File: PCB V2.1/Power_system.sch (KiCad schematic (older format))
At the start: 18 parts, among them J3 B2B-PH-K-S(LF)(SN), J4 B3B-PH-K-S(LF)(SN), Q1 DMG2307L-7, Q2 DMG2307L-7, U2 BQ24210DQCT, U3 AZ1117CR-3.3TRG1_1

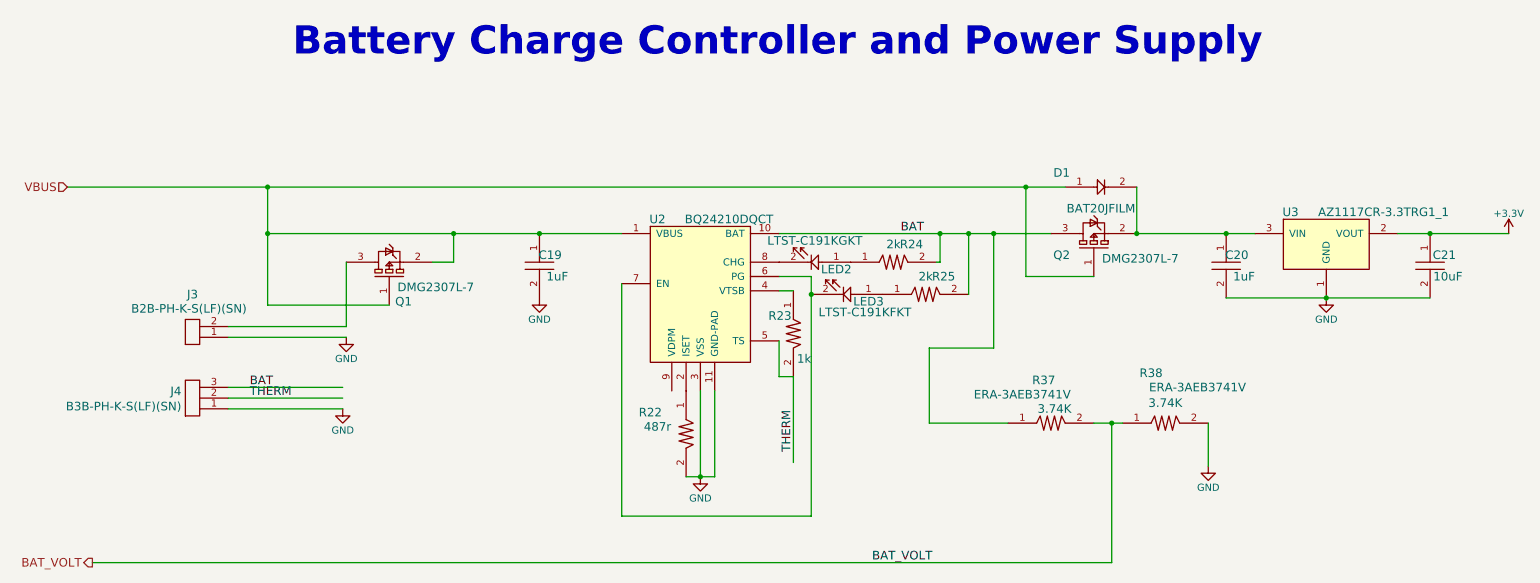
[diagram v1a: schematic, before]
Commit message: Test Points
Test points added as well as some retooling of the PCB overall. More
updates to come before the pending fab
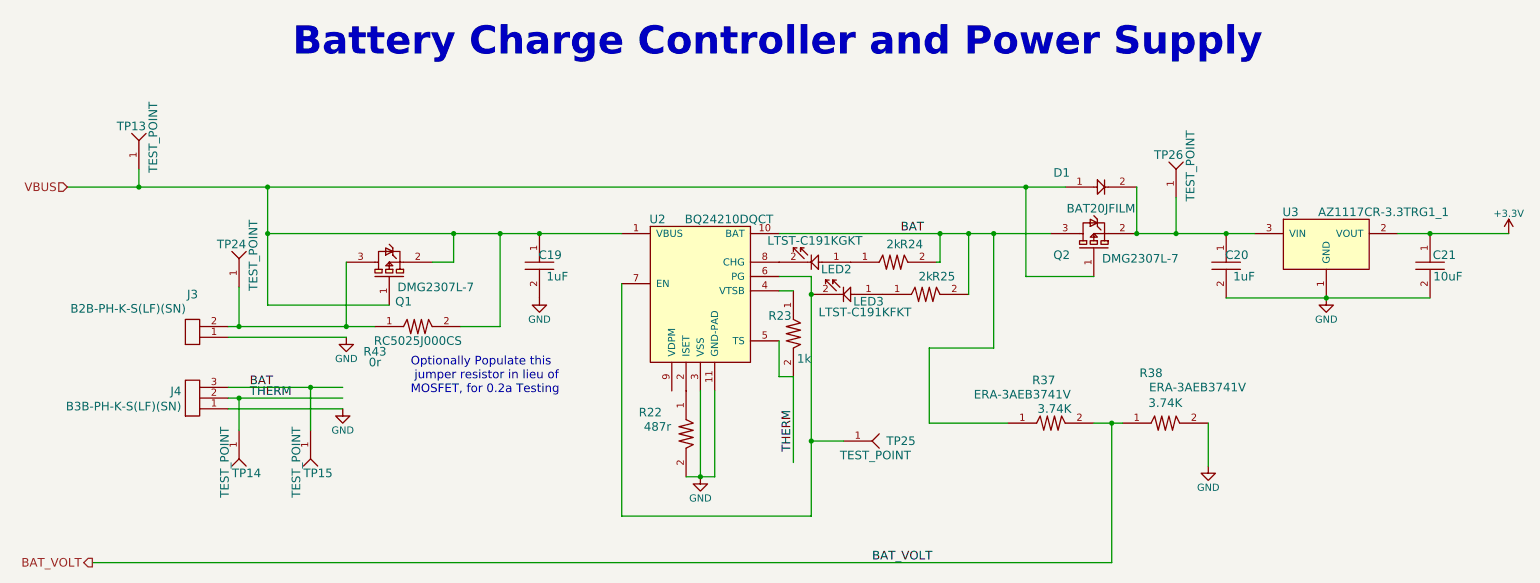
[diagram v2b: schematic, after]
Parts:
- added R43: RC5025J000CS, PCB_Footprints:R2010, symbol RC5025J000CS
- added TP13, TP14, TP15, TP24, TP25, TP26: TEST_POINT, PCB_Footprints:TEST_POINT, symbol TEST_POINT
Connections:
- wire segments 41 -> 49
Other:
- note added: "Optionally Populate this\n jumper resistor in lieu of \nMOSFET, for 0.2a Testing"
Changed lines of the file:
@@
 	-1   0    0    1
 $EndComp
-Wire Wire Line
-	800  2575 7775 2575
-Wire Wire Line
-	2200 2575 2200 3400
-Wire Wire Line
-	2200 2900 4675 2900
-Wire Wire Line
-	5775 2900 7675 2900
-Wire Wire Line
-	8275 2575 8275 2900
-Connection ~ 2200 2575
-Wire Wire Line
-	7975 3200 7500 3200
-Wire Wire Line
-	7500 3200 7500 2575
-Connection ~ 7500 2575
-Wire Wire Line
-	8275 2900 9100 2900
-Wire Wire Line
-	10100 2900 10875 2900
-Connection ~ 10325 2900
-$Comp
-L +3.3V #PWR41
+$Comp
+L +3.3V #PWR40
 U 1 1 57D80E79
 P 10875 2900
-F 0 "#PWR41" H 10875 2750 50  0001 C CNN
+F 0 "#PWR40" H 10875 2750 50  0001 C CNN
 F 1 "+3.3V" H 10875 3040 50  0000 C CNN
 F 2 "" H 10875 2900 50  0000 C CNN
@@
 $EndComp
 $Comp
-L GND #PWR40
+L GND #PWR39
 U 1 1 57D80F19
 P 9600 3350
-F 0 "#PWR40" H 9600 3100 50  0001 C CNN
+F 0 "#PWR39" H 9600 3100 50  0001 C CNN
 F 1 "GND" H 9600 3200 50  0000 C CNN
 F 2 "" H 9600 3350 50  0000 C CNN
@@
 	1    0    0    -1
 $EndComp
-Wire Wire Line
-	8900 3350 10325 3350
-Connection ~ 9600 3350
-Connection ~ 8900 2900
-Connection ~ 8275 2900
-Wire Wire Line
-	6900 2900 6900 3100
-Connection ~ 6900 2900
-Wire Wire Line
-	7100 3325 7100 2900
-Connection ~ 7100 2900
-Wire Wire Line
-	6900 3100 6875 3100
-Wire Wire Line
-	5775 3200 6000 3200
-Wire Wire Line
-	6000 3200 6000 4875
-Wire Wire Line
-	6000 4875 4675 4875
-Wire Wire Line
-	4675 4875 4675 3250
-Connection ~ 6000 3325
-$Comp
-L GND #PWR38
+$Comp
+L GND #PWR37
 U 1 1 57D82F5E
 P 5225 4600
-F 0 "#PWR38" H 5225 4350 50  0001 C CNN
+F 0 "#PWR37" H 5225 4350 50  0001 C CNN
 F 1 "GND" H 5225 4450 50  0000 C CNN
 F 2 "" H 5225 4600 50  0000 C CNN
@@
 	1    0    0    -1
 $EndComp
-Wire Wire Line
-	5225 4000 5225 4600
-Wire Wire Line
-	5125 4600 5325 4600
-Wire Wire Line
-	5325 4600 5325 4000
-Connection ~ 5225 4600
-Wire Wire Line
-	5875 3300 5775 3300
-Wire Wire Line
-	5775 3650 5775 3900
-Wire Wire Line
-	5775 3900 5875 3900
-Wire Wire Line
-	5875 3900 5875 4500
 Text Label 5875 4425 1    60   ~ 0
 THERM
@@
 $EndComp
 $Comp
-L GND #PWR37
+L GND #PWR36
 U 1 1 57D853F5
 P 4100 3350
-F 0 "#PWR37" H 4100 3100 50  0001 C CNN
+F 0 "#PWR36" H 4100 3100 50  0001 C CNN
 F 1 "GND" H 4100 3200 50  0000 C CNN
 F 2 "" H 4100 3350 50  0000 C CNN
@@
 $EndComp
 $Comp
-L GND #PWR36
+L GND #PWR35
 U 1 1 57D89874
 P 2750 3625
-F 0 "#PWR36" H 2750 3375 50  0001 C CNN
+F 0 "#PWR35" H 2750 3375 50  0001 C CNN
 F 1 "GND" H 2750 3475 50  0000 C CNN
 F 2 "" H 2750 3625 50  0000 C CNN
@@
 	1    0    0    -1
 $EndComp
-Wire Wire Line
-	1925 3625 2750 3625
-Connection ~ 3500 2900
 $Comp
 L DMG2307L-7 Q1
@@
 	0    -1   -1   0
 $EndComp
-Wire Wire Line
-	1925 3550 2750 3550
-Wire Wire Line
-	2750 3550 2750 3100
-Wire Wire Line
-	3350 3100 3500 3100
-Wire Wire Line
-	3500 3100 3500 2900
-Wire Wire Line
-	2200 3400 3050 3400
-Connection ~ 2200 2900
-$Comp
-L GND #PWR35
+$Comp
+L GND #PWR34
 U 1 1 57D8ABE6
 P 2725 4125
-F 0 "#PWR35" H 2725 3875 50  0001 C CNN
+F 0 "#PWR34" H 2725 3875 50  0001 C CNN
 F 1 "GND" H 2725 3975 50  0000 C CNN
 F 2 "" H 2725 4125 50  0000 C CNN
@@
 	1    0    0    -1
 $EndComp
-Wire Wire Line
-	2725 4125 1925 4125
-Wire Wire Line
-	1925 4050 2725 4050
-Wire Wire Line
-	1925 3975 2725 3975
 Text Label 2075 3975 0    60   ~ 0
 BAT
@@
 P 1725 3550
 F 0 "J3" H 1675 3325 60  0000 C CNN
-F 1 "B2B-PH-K-S(LF)(SN)" H 1650 3425 60  0000 C CNN
+F 1 "B2B-PH-K-S(LF)(SN)" H 1225 3425 60  0000 C CNN
 F 2 "PCB_Footprints:B2B-PH-K-S(LF)(SN)" H 1575 3625 60  0001 C CNN
 F 3 "http://www.jst-mfg.com/product/pdf/eng/ePH.pdf" H 1450 3925 60  0001 C CNN
@@
 	1    0    0    1
 $EndComp
-Connection ~ 4100 2900
 $Comp
 L ERA-3AEB3741V R37
@@
 $EndComp
 $Comp
-L GND #PWR39
+L GND #PWR38
 U 1 1 57E05471
 P 8775 4525
-F 0 "#PWR39" H 8775 4275 50  0001 C CNN
+F 0 "#PWR38" H 8775 4275 50  0001 C CNN
 F 1 "GND" H 8775 4375 50  0000 C CNN
 F 2 "" H 8775 4525 50  0000 C CNN
@@
 	1    0    0    -1
 $EndComp
-Wire Wire Line
-	8775 4225 8775 4525
-Wire Wire Line
-	7975 4225 8175 4225
-Wire Wire Line
-	8100 4225 8100 5200
-Wire Wire Line
-	8100 5200 975  5200
-Connection ~ 8100 4225
-Wire Wire Line
-	7375 4225 6825 4225
-Wire Wire Line
-	6825 4225 6825 3700
-Wire Wire Line
-	6825 3700 7275 3700
-Wire Wire Line
-	7275 3700 7275 2900
-Connection ~ 7275 2900
 Text Label 6425 5200 0    60   ~ 0
 BAT_VOLT
 Text HLabel 975  5200 0    60   Output ~ 0
 BAT_VOLT
+Text Notes 3200 4025 0    60   ~ 0
+Optionally Populate this\n jumper resistor in lieu of \nMOSFET, for 0.2a Testing
+$Comp
+L RC5025J000CS R43
+U 1 1 57F3616C
+P 3250 3550
+F 0 "R43" H 2950 3375 60  0000 C CNN
+F 1 "RC5025J000CS" H 3250 3450 60  0000 C CNN
+F 2 "PCB_Footprints:R2010" H 2850 3800 60  0001 C CNN
+F 3 "https://media.digikey.com/pdf/Data%20Sheets/Samsung%20PDFs/RC_Series_ds.pdf" H 2950 4000 60  0001 C CNN
+F 4 "0.02113 @ 1000" H 4800 5500 60  0001 C CNN "Cost"
+F 5 "3 Oct 2016" H 3150 4100 60  0001 C CNN "Date Created"
+F 6 "3 Oct 2016" H 3250 4200 60  0001 C CNN "Date Modified"
+F 7 "Adam Vadala-Roth" H 3350 4300 60  0001 C CNN "Designer"
+F 8 "0.4mm" H 3450 4400 60  0001 C CNN "Height"
+F 9 "Yes" H 3550 4500 60  0001 C CNN "RHoS?"
+F 10 "Samsung Electro-Mechanics America, Inc." H 3650 4600 60  0001 C CNN "MFR"
+F 11 "RC5025J000CS" H 3750 4700 60  0001 C CNN "MFR#"
+F 12 "SMT/SMD" H 3850 4800 60  0001 C CNN "Mounting"
+F 13 "2" H 3950 4900 60  0001 C CNN "Pin Count#"
+F 14 "Active" H 4050 5000 60  0001 C CNN "Status"
+F 15 "%" H 4150 5100 60  0001 C CNN "Tolerance"
+F 16 "passive" H 4250 5200 60  0001 C CNN "Type"
+F 17 "N/A" H 4350 5300 60  0001 C CNN "Voltage"
+F 18 "1" H 4450 5400 60  0001 C CNN "Wattage"
+F 19 "0r" H 2950 3300 60  0000 C CNN "Component-Value"
+F 20 "RES SMD 0.0 OHM JUMPER 2/3W 2010" H 4650 5600 60  0001 C CNN "Description"
+	1    3250 3550
+	1    0    0    -1
+$EndComp
+$Comp
+L TEST_POINT TP14
+U 1 1 57F526A8
+P 2000 4400
+F 0 "TP14" V 2175 4350 60  0000 L CNN
+F 1 "TEST_POINT" H 1850 4300 60  0000 L CNN
+F 2 "PCB_Footprints:TEST_POINT" H 2175 4675 60  0001 C CNN
+F 3 "" H 2075 4400 60  0001 C CNN
+	1    2000 4400
+	0    1    1    0
+$EndComp
+$Comp
+L TEST_POINT TP15
+U 1 1 57F52C57
+P 2500 4400
+F 0 "TP15" V 2675 4350 60  0000 L CNN
+F 1 "TEST_POINT" H 2350 4300 60  0000 L CNN
+F 2 "PCB_Footprints:TEST_POINT" H 2675 4675 60  0001 C CNN
+F 3 "" H 2575 4400 60  0001 C CNN
+	1    2500 4400
+	0    1    1    0
+$EndComp
+$Comp
+L TEST_POINT TP13
+U 1 1 57F533A0
+P 1300 2325
+F 0 "TP13" V 1475 2275 60  0000 L CNN
+F 1 "TEST_POINT" H 1150 2225 60  0000 L CNN
+F 2 "PCB_Footprints:TEST_POINT" H 1475 2600 60  0001 C CNN
+F 3 "" H 1375 2325 60  0001 C CNN
+	1    1300 2325
+	0    -1   -1   0
+$EndComp
+$Comp
+L TEST_POINT TP24
+U 1 1 57F59EE1
+P 2000 3150
+F 0 "TP24" V 2175 3100 60  0000 L CNN
+F 1 "TEST_POINT" H 1850 3050 60  0000 L CNN
+F 2 "PCB_Footprints:TEST_POINT" H 2175 3425 60  0001 C CNN
+F 3 "" H 2075 3150 60  0001 C CNN
+	1    2000 3150
+	0    -1   -1   0
+$EndComp
+Wire Wire Line
+	800  2575 7775 2575
+Wire Wire Line
+	2200 2575 2200 3400
+Wire Wire Line
+	2200 2900 4675 2900
+Wire Wire Line
+	5775 2900 7675 2900
+Wire Wire Line
+	8275 2575 8275 2900
+Connection ~ 2200 2575
+Wire Wire Line
+	7975 3200 7500 3200
+Wire Wire Line
+	7500 3200 7500 2575
+Connection ~ 7500 2575
+Wire Wire Line
+	8275 2900 9100 2900
+Wire Wire Line
+	10100 2900 10875 2900
+Connection ~ 10325 2900
+Wire Wire Line
+	8900 3350 10325 3350
+Connection ~ 9600 3350
+Connection ~ 8900 2900
+Connection ~ 8275 2900
+Wire Wire Line
+	6900 2900 6900 3100
+Connection ~ 6900 2900
+Wire Wire Line
+	7100 3325 7100 2900
+Connection ~ 7100 2900
+Wire Wire Line
+	6900 3100 6875 3100
+Wire Wire Line
+	5775 3200 6000 3200
+Wire Wire Line
+	6000 3200 6000 4875
+Wire Wire Line
+	6000 4875 4675 4875
+Wire Wire Line
+	4675 4875 4675 3250
+Connection ~ 6000 3325
+Wire Wire Line
+	5225 4000 5225 4600
+Wire Wire Line
+	5125 4600 5325 4600
+Wire Wire Line
+	5325 4600 5325 4000
+Connection ~ 5225 4600
+Wire Wire Line
+	5875 3300 5775 3300
+Wire Wire Line
+	5775 3650 5775 3900
+Wire Wire Line
+	5775 3900 5875 3900
+Wire Wire Line
+	5875 3900 5875 4500
+Wire Wire Line
+	1925 3625 2750 3625
+Connection ~ 3500 2900
+Wire Wire Line
+	1925 3550 2950 3550
+Wire Wire Line
+	2750 3550 2750 3100
+Wire Wire Line
+	3350 3100 3500 3100
+Wire Wire Line
+	3500 3100 3500 2900
+Wire Wire Line
+	2200 3400 3050 3400
+Connection ~ 2200 2900
+Wire Wire Line
+	2725 4125 1925 4125
+Wire Wire Line
+	1925 4050 2725 4050
+Wire Wire Line
+	1925 3975 2725 3975
+Connection ~ 4100 2900
+Wire Wire Line
+	8775 4225 8775 4525
+Wire Wire Line
+	7975 4225 8175 4225
+Wire Wire Line
+	8100 4225 8100 5200
+Wire Wire Line
+	8100 5200 975  5200
+Connection ~ 8100 4225
+Wire Wire Line
+	7375 4225 6825 4225
+Wire Wire Line
+	6825 4225 6825 3700
+Wire Wire Line
+	6825 3700 7275 3700
+Wire Wire Line
+	7275 3700 7275 2900
+Connection ~ 7275 2900
+Connection ~ 2750 3550
+Wire Wire Line
+	3550 3550 3825 3550
+Wire Wire Line
+	3825 3550 3825 2900
+Connection ~ 3825 2900
+Wire Wire Line
+	2000 4275 2000 4050
+Connection ~ 2000 4050
+Wire Wire Line
+	2500 4275 2500 3975
+Connection ~ 2500 3975
+Wire Wire Line
+	1300 2450 1300 2575
+Connection ~ 1300 2575
+Wire Wire Line
+	2000 3275 2000 3550
+Connection ~ 2000 3550
+$Comp
+L TEST_POINT TP26
+U 1 1 57F5A982
+P 8550 2525
+F 0 "TP26" V 8725 2475 60  0000 L CNN
+F 1 "TEST_POINT" H 8400 2425 60  0000 L CNN
+F 2 "PCB_Footprints:TEST_POINT" H 8725 2800 60  0001 C CNN
+F 3 "" H 8625 2525 60  0001 C CNN
+	1    8550 2525
+	0    -1   -1   0
+$EndComp
+Wire Wire Line
+	8550 2650 8550 2900
+Connection ~ 8550 2900
+$Comp
+L TEST_POINT TP25
+U 1 1 57F5BE97
+P 6350 4350
+F 0 "TP25" H 6525 4350 60  0000 L CNN
+F 1 "TEST_POINT" H 6200 4250 60  0000 L CNN
+F 2 "PCB_Footprints:TEST_POINT" H 6525 4625 60  0001 C CNN
+F 3 "" H 6425 4350 60  0001 C CNN
+	1    6350 4350
+	1    0    0    -1
+$EndComp
+Wire Wire Line
+	6225 4350 6000 4350
+Connection ~ 6000 4350
 $EndSCHEMATC

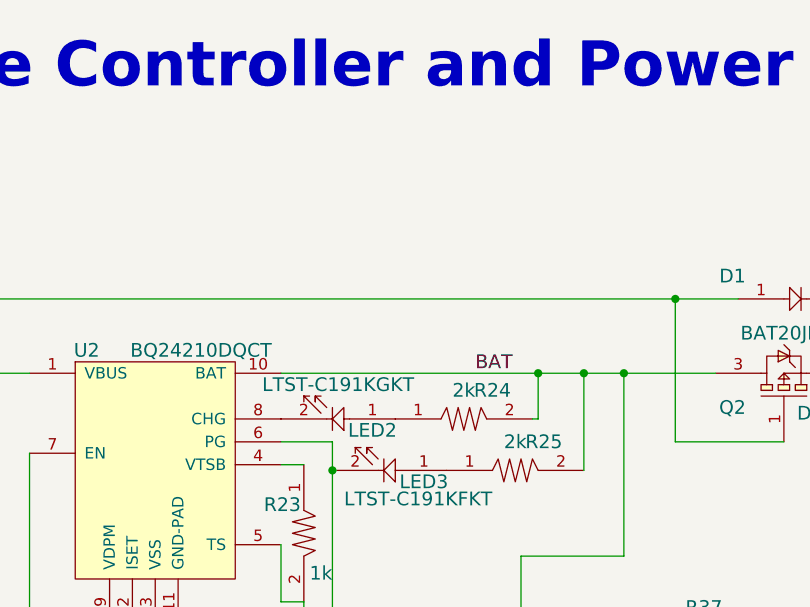
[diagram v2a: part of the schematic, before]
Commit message: JTAG Test Points
Test Points added to JTAG.
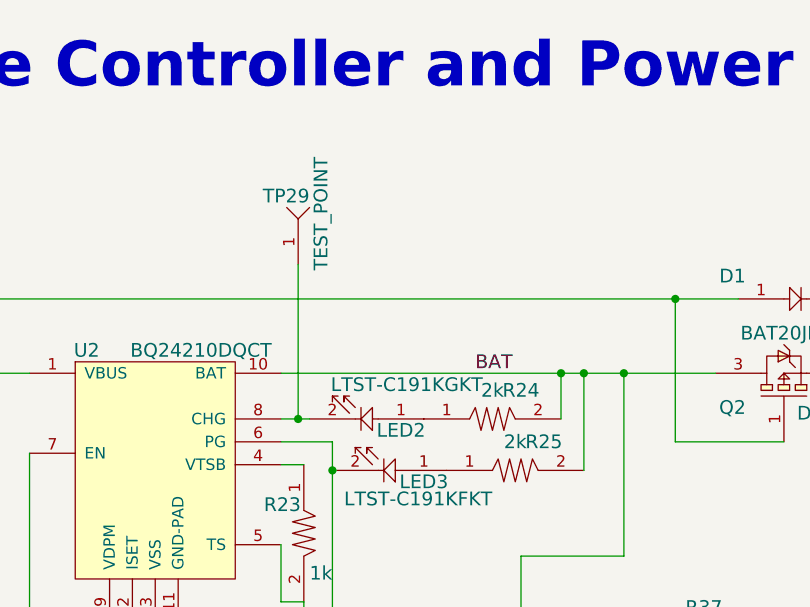
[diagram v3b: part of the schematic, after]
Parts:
- added TP29: TEST_POINT, PCB_Footprints:TEST_POINT, symbol TEST_POINT
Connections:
- wire segments 49 -> 50
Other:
- moved on the sheet: LED2, R24
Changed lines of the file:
@@
 L LTST-C191KGKT LED2
 U 1 1 57D7EE0F
-P 6025 3100
-F 0 "LED2" H 5875 3150 60  0000 C CNN
-F 1 "LTST-C191KGKT" H 6025 2950 60  0000 C CNN
-F 2 "PCB_Footprints:LED0603" H 7450 5025 60  0001 C CNN
-F 3 "http://optoelectronics.liteon.com/upload/download/DS22-2000-228/S_110_LTST-C191KGKT.pdf" H 7650 5150 60  0001 C CNN
-F 4 "0.04040 @ 5000" H 5875 3300 60  0001 C CNN "Cost"
-F 5 "8 Sept 2016" H 5975 3400 60  0001 C CNN "Date Created"
-F 6 "8 Sept 2016" H 6075 3500 60  0001 C CNN "Date Modified"
-F 7 "Adam Vadala-Roth" H 6175 3600 60  0001 C CNN "Designer"
-F 8 "0.55mm" H 6275 3700 60  0001 C CNN "Height"
-F 9 "Yes" H 6375 3800 60  0001 C CNN "RhoS?"
-F 10 "Lite-On Inc" H 6475 3900 60  0001 C CNN "MFR"
-F 11 "LTST-C191KGKT" H 6575 4000 60  0001 C CNN "MFR#"
-F 12 "SMT/SMD" H 6675 4100 60  0001 C CNN "Mounting"
-F 13 "2" H 6775 4200 60  0001 C CNN "Pin Count#"
-F 14 "Active" H 6875 4300 60  0001 C CNN "Status"
-F 15 "N/A" H 6975 4400 60  0001 C CNN "Tolerance"
-F 16 "0603 LED" H 7075 4500 60  0001 C CNN "Type"
-F 17 "N/A" H 7175 4600 60  0001 C CNN "Voltage"
-F 18 "N/A" H 7275 4700 60  0001 C CNN "Wattage"
-F 19 "N/A" H 7375 4800 60  0001 C CNN "Component-Value"
-F 20 "Green 571nm LED Indication - Discrete 2V 0603 (1608 Metric)" H 7475 4900 60  0001 C CNN "Description"
-	1    6025 3100
+P 6150 3100
+F 0 "LED2" H 6000 3150 60  0000 C CNN
+F 1 "LTST-C191KGKT" H 5975 2950 60  0000 C CNN
+F 2 "PCB_Footprints:LED0603" H 7575 5025 60  0001 C CNN
+F 3 "http://optoelectronics.liteon.com/upload/download/DS22-2000-228/S_110_LTST-C191KGKT.pdf" H 7775 5150 60  0001 C CNN
+F 4 "0.04040 @ 5000" H 6000 3300 60  0001 C CNN "Cost"
+F 5 "8 Sept 2016" H 6100 3400 60  0001 C CNN "Date Created"
+F 6 "8 Sept 2016" H 6200 3500 60  0001 C CNN "Date Modified"
+F 7 "Adam Vadala-Roth" H 6300 3600 60  0001 C CNN "Designer"
+F 8 "0.55mm" H 6400 3700 60  0001 C CNN "Height"
+F 9 "Yes" H 6500 3800 60  0001 C CNN "RhoS?"
+F 10 "Lite-On Inc" H 6600 3900 60  0001 C CNN "MFR"
+F 11 "LTST-C191KGKT" H 6700 4000 60  0001 C CNN "MFR#"
+F 12 "SMT/SMD" H 6800 4100 60  0001 C CNN "Mounting"
+F 13 "2" H 6900 4200 60  0001 C CNN "Pin Count#"
+F 14 "Active" H 7000 4300 60  0001 C CNN "Status"
+F 15 "N/A" H 7100 4400 60  0001 C CNN "Tolerance"
+F 16 "0603 LED" H 7200 4500 60  0001 C CNN "Type"
+F 17 "N/A" H 7300 4600 60  0001 C CNN "Voltage"
+F 18 "N/A" H 7400 4700 60  0001 C CNN "Wattage"
+F 19 "N/A" H 7500 4800 60  0001 C CNN "Component-Value"
+F 20 "Green 571nm LED Indication - Discrete 2V 0603 (1608 Metric)" H 7600 4900 60  0001 C CNN "Description"
+	1    6150 3100
 	-1   0    0    1
 $EndComp
@@
 L RC1608J202CS R24
 U 1 1 57DA18C7
-P 6575 3100
-F 0 "R24" H 6700 3225 60  0000 C CNN
-F 1 "RC1608J202CS" H 6575 3347 60  0001 C CNN
-F 2 "PCB_Footprints:R0603" H 6175 3350 60  0001 C CNN
-F 3 "https://media.digikey.com/pdf/Data%20Sheets/Samsung%20PDFs/RC_Series_ds.pdf" H 6275 3550 60  0001 C CNN
-F 4 "0.00268 @ 5000" H 8125 5050 60  0001 C CNN "Cost"
-F 5 "14 Sept 2016" H 6475 3650 60  0001 C CNN "Date Created"
-F 6 "14 Sept 2016" H 6575 3750 60  0001 C CNN "Date Modified"
-F 7 "Adam Vadala-Roth" H 6675 3850 60  0001 C CNN "Designer"
-F 8 "0.55mm" H 6775 3950 60  0001 C CNN "Height"
-F 9 "Yes" H 6875 4050 60  0001 C CNN "RHoS?"
-F 10 "Samsung Electro-Mechanics America, Inc." H 6975 4150 60  0001 C CNN "MFR"
-F 11 "RC1608F202CS" H 7075 4250 60  0001 C CNN "MFR#"
-F 12 "SMT/SMD" H 7175 4350 60  0001 C CNN "Mounting"
-F 13 "2" H 7275 4450 60  0001 C CNN "Pin Count#"
-F 14 "Active" H 7375 4550 60  0001 C CNN "Status"
-F 15 "1%" H 7475 4650 60  0001 C CNN "Tolerance"
-F 16 "passive" H 7575 4750 60  0001 C CNN "Type"
-F 17 "N/A" H 7675 4850 60  0001 C CNN "Voltage"
-F 18 "1/10" H 7775 4950 60  0001 C CNN "Wattage"
-F 19 "2k" H 6575 3225 60  0000 C CNN "Component-Value"
-F 20 "RES SMD 2K OHM 1% 1/10W 0603" H 7975 5150 60  0001 C CNN "Description"
-	1    6575 3100
+P 6700 3100
+F 0 "R24" H 6825 3225 60  0000 C CNN
+F 1 "RC1608J202CS" H 6700 3347 60  0001 C CNN
+F 2 "PCB_Footprints:R0603" H 6300 3350 60  0001 C CNN
+F 3 "https://media.digikey.com/pdf/Data%20Sheets/Samsung%20PDFs/RC_Series_ds.pdf" H 6400 3550 60  0001 C CNN
+F 4 "0.00268 @ 5000" H 8250 5050 60  0001 C CNN "Cost"
+F 5 "14 Sept 2016" H 6600 3650 60  0001 C CNN "Date Created"
+F 6 "14 Sept 2016" H 6700 3750 60  0001 C CNN "Date Modified"
+F 7 "Adam Vadala-Roth" H 6800 3850 60  0001 C CNN "Designer"
+F 8 "0.55mm" H 6900 3950 60  0001 C CNN "Height"
+F 9 "Yes" H 7000 4050 60  0001 C CNN "RHoS?"
+F 10 "Samsung Electro-Mechanics America, Inc." H 7100 4150 60  0001 C CNN "MFR"
+F 11 "RC1608F202CS" H 7200 4250 60  0001 C CNN "MFR#"
+F 12 "SMT/SMD" H 7300 4350 60  0001 C CNN "Mounting"
+F 13 "2" H 7400 4450 60  0001 C CNN "Pin Count#"
+F 14 "Active" H 7500 4550 60  0001 C CNN "Status"
+F 15 "1%" H 7600 4650 60  0001 C CNN "Tolerance"
+F 16 "passive" H 7700 4750 60  0001 C CNN "Type"
+F 17 "N/A" H 7800 4850 60  0001 C CNN "Voltage"
+F 18 "1/10" H 7900 4950 60  0001 C CNN "Wattage"
+F 19 "2k" H 6700 3225 60  0000 C CNN "Component-Value"
+F 20 "RES SMD 2K OHM 1% 1/10W 0603" H 8100 5150 60  0001 C CNN "Description"
+	1    6700 3100
 	1    0    0    -1
 $EndComp
@@
 Connection ~ 8275 2900
 Wire Wire Line
-	6900 2900 6900 3100
-Connection ~ 6900 2900
+	7000 2900 7000 3100
+Connection ~ 7000 2900
 Wire Wire Line
 	7100 3325 7100 2900
 Connection ~ 7100 2900
-Wire Wire Line
-	6900 3100 6875 3100
 Wire Wire Line
 	5775 3200 6000 3200
@@
 	6225 4350 6000 4350
 Connection ~ 6000 4350
+$Comp
+L TEST_POINT TP29
+U 1 1 57F68AD2
+P 5850 2300
+F 0 "TP29" V 6025 2250 60  0000 L CNN
+F 1 "TEST_POINT" H 5700 2200 60  0000 L CNN
+F 2 "PCB_Footprints:TEST_POINT" H 6025 2575 60  0001 C CNN
+F 3 "" H 5925 2300 60  0001 C CNN
+	1    5850 2300
+	0    -1   -1   0
+$EndComp
+Wire Wire Line
+	5775 3100 5900 3100
+Wire Wire Line
+	5850 2425 5850 3100
+Connection ~ 5850 3100
 $EndSCHEMATC
